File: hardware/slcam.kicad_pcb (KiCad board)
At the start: 4 copper layers, 42.2 x 25.4 mm, 33 parts, among them J1 532610671, J2 Conn_01x08, J3 Conn_01x04, J4 532610371, J5 532610371, U1 STM32F103C8Tx, U2 W25Q128JVS, U3 TCAN330G, U4 TPS2044D, Y1 Crystal_GND24

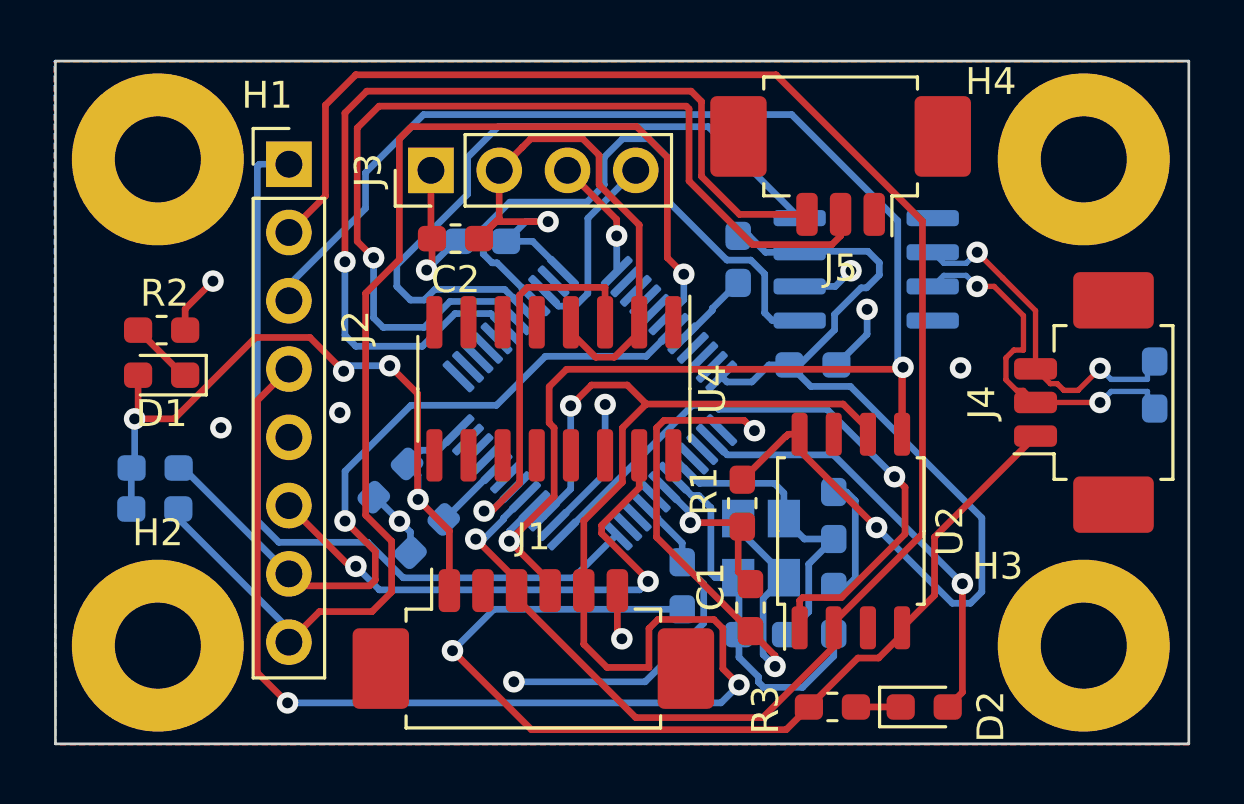
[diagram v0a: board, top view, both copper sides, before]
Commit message: hardware: Fixing DRC warnings #29
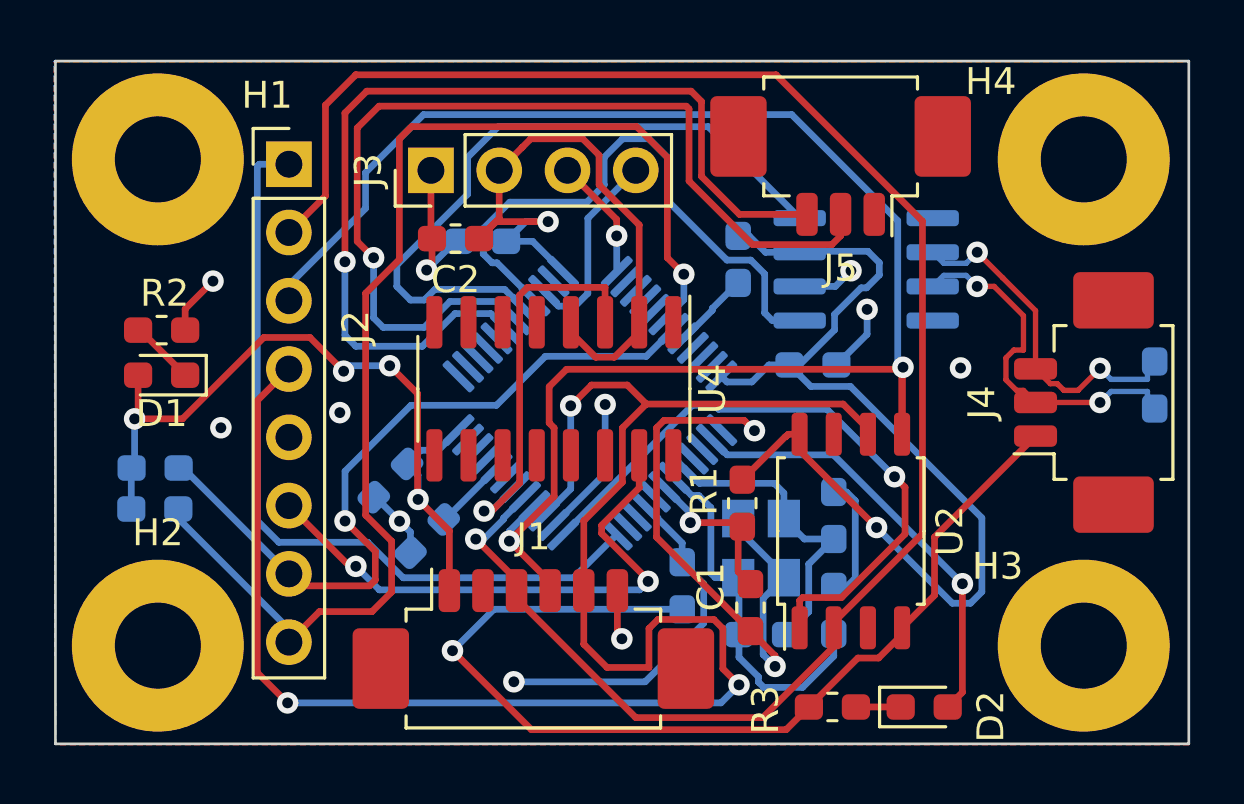
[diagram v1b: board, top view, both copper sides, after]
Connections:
- U1 pad 1: Net-(U1-Pad1) -> unconnected-(U1-Pad1)
- U1 pad 10: Net-(U1-Pad10) -> unconnected-(U1-Pad10)
- U1 pad 11: Net-(U1-Pad11) -> unconnected-(U1-Pad11)
- U1 pad 19: Net-(U1-Pad19) -> unconnected-(U1-Pad19)
- U1 pad 21: Net-(U1-Pad21) -> unconnected-(U1-Pad21)
- U1 pad 22: Net-(U1-Pad22) -> unconnected-(U1-Pad22)
- U1 pad 23: Net-(U1-Pad23) -> unconnected-(U1-Pad23)
- U1 pad 25: Net-(U1-Pad25) -> unconnected-(U1-Pad25)
- U1 pad 26: Net-(U1-Pad26) -> unconnected-(U1-Pad26)
- U1 pad 27: Net-(U1-Pad27) -> unconnected-(U1-Pad27)
- U1 pad 28: Net-(U1-Pad28) -> unconnected-(U1-Pad28)
- U1 pad 29: Net-(U1-Pad29) -> unconnected-(U1-Pad29)
- U1 pad 3: Net-(U1-Pad3) -> unconnected-(U1-Pad3)
- U1 pad 35: Net-(U1-Pad35) -> unconnected-(U1-Pad35)
- U1 pad 38: Net-(U1-Pad38) -> unconnected-(U1-Pad38)
- U1 pad 39: Net-(U1-Pad39) -> unconnected-(U1-Pad39)
- U1 pad 4: Net-(U1-Pad4) -> unconnected-(U1-Pad4)
- U1 pad 40: Net-(U1-Pad40) -> unconnected-(U1-Pad40)
- U1 pad 41: Net-(U1-Pad41) -> unconnected-(U1-Pad41)
- U1 pad 45: Net-(U1-Pad45) -> unconnected-(U1-Pad45)
- U1 pad 46: Net-(U1-Pad46) -> unconnected-(U1-Pad46)
- U1 pad 47: Net-(U1-Pad47) -> unconnected-(U1-Pad47)
- U1 pad 8: Net-(U1-Pad8) -> unconnected-(U1-Pad8)
- U2 pad 3: Net-(U2-Pad3) -> unconnected-(U2-Pad3)
- U2 pad 7: Net-(U2-Pad7) -> unconnected-(U2-Pad7)
- U3 pad 5: Net-(U3-Pad5) -> unconnected-(U3-Pad5)
- U3 pad 8: Net-(U3-Pad8) -> unconnected-(U3-Pad8)
- U4 pad 13: Net-(U4-Pad13) -> unconnected-(U4-Pad13)
- U4 pad 14: Net-(U4-Pad14) -> unconnected-(U4-Pad14)
- U4 pad 16: Net-(U4-Pad16) -> unconnected-(U4-Pad16)
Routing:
- net GND: track 145.4 -> 144.3 mm
- net VCC: track 108.4 -> 107.5 mm

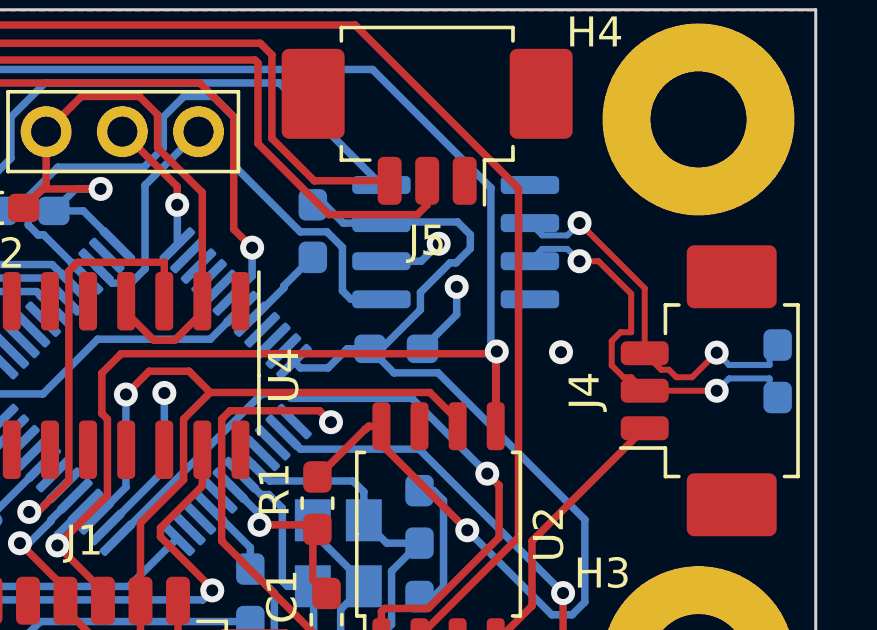
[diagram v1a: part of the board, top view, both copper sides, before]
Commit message: hardware: Adding the project name/version and the SpaceLab logo to the PCB #23 #29 closes #38 closes #42
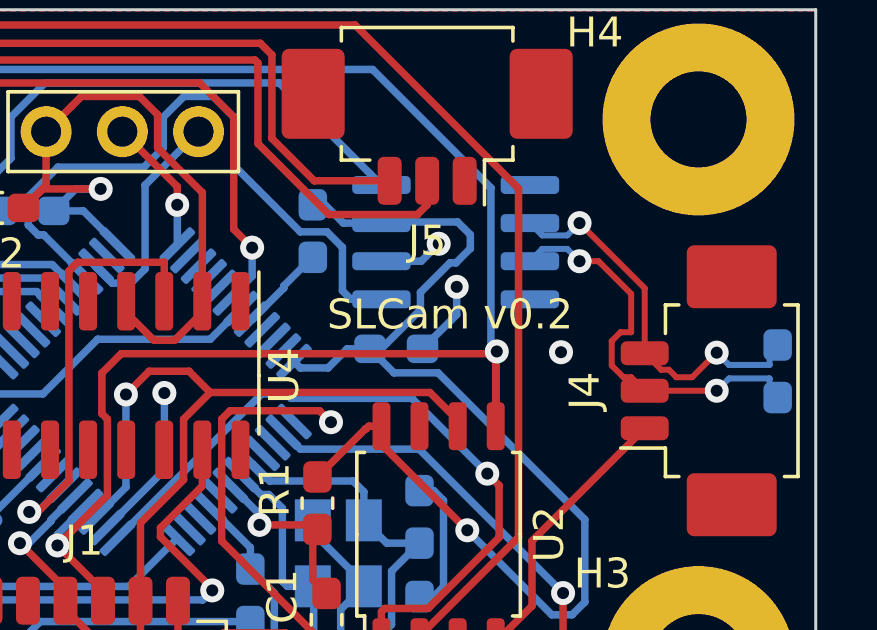
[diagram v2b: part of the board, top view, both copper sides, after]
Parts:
- added G***: LOGO, lib:spacelab-logo, B.Cu at (233.7, 62.5)
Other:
- board text added: "SLCam v0.2"

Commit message: hardware: Adding a table with info about the PCB to the layout project #29
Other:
- board text added: "0.2000 mm / 0.0000 mm"
- board text added: "0.3000 mm"
- board text added: "1.6600 mm"
- board text added: "4"
- board text added: "42.1640 mm x 25.4000 mm"
- board text added: "BOARD CHARACTERISTICS"
- board text added: "Board Thickness:"
- board text added: "Board overall dimensions:"
- board text added: "Castellated pads:"
- board text added: "Copper Finish:"
- board text added: "Copper Layer Count:"
- board text added: "Edge card connectors:"
- board text added: "Impedance Control:"
- board text added: "Min hole diameter:"
- board text added: "Min track/spacing:"
- board text added: "No"
- board text added: "None"
- board text added: "Plated Board Edge:"
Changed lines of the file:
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@@
     (effects (font (size 1 1) (thickness 0.15)))
+  )
+  (gr_text "No" (at 51.087143 37.416) (layer "Dwgs.User")
+    (effects (font (size 1.5 1.5) (thickness 0.2)) (justify left top))
+  )
+  (gr_text "42.1640 mm x 25.4000 mm" (at 51.087143 24.771) (layer "Dwgs.User")
+    (effects (font (size 1.5 1.5) (thickness 0.2)) (justify left top))
+  )
+  (gr_text "Copper Layer Count: " (at 18.53 20.556) (layer "Dwgs.User")
+    (effects (font (size 1.5 1.5) (thickness 0.2)) (justify left top))
+  )
+  (gr_text "1.6600 mm" (at 109.987143 20.556) (layer "Dwgs.User")
+    (effects (font (size 1.5 1.5) (thickness 0.2)) (justify left top))
+  )
+  (gr_text "No" (at 51.087143 41.631) (layer "Dwgs.User")
+    (effects (font (size 1.5 1.5) (thickness 0.2)) (justify left top))
+  )
+  (gr_text "Min hole diameter: " (at 85.144286 28.986) (layer "Dwgs.User")
+    (effects (font (size 1.5 1.5) (thickness 0.2)) (justify left top))
+  )
+  (gr_text "Edge card connectors: " (at 18.53 41.631) (layer "Dwgs.User")
+    (effects (font (size 1.5 1.5) (thickness 0.2)) (justify left top))
+  )
+  (gr_text "4" (at 51.087143 20.556) (layer "Dwgs.User")
+    (effects (font (size 1.5 1.5) (thickness 0.2)) (justify left top))
+  )
+  (gr_text "0.3000 mm" (at 109.987143 28.986) (layer "Dwgs.User")
+    (effects (font (size 1.5 1.5) (thickness 0.2)) (justify left top))
+  )
+  (gr_text "0.2000 mm / 0.0000 mm" (at 51.087143 28.986) (layer "Dwgs.User")
+    (effects (font (size 1.5 1.5) (thickness 0.2)) (justify left top))
+  )
+  (gr_text "No" (at 109.987143 37.416) (layer "Dwgs.User")
+    (effects (font (size 1.5 1.5) (thickness 0.2)) (justify left top))
+  )
+  (gr_text "" (at 85.144286 24.771) (layer "Dwgs.User")
+    (effects (font (size 1.5 1.5) (thickness 0.2)) (justify left top))
+  )
+  (gr_text "Plated Board Edge: " (at 85.144286 37.416) (layer "Dwgs.User")
+    (effects (font (size 1.5 1.5) (thickness 0.2)) (justify left top))
+  )
+  (gr_text "Castellated pads: " (at 18.53 37.416) (layer "Dwgs.User")
+    (effects (font (size 1.5 1.5) (thickness 0.2)) (justify left top))
+  )
+  (gr_text "No" (at 109.987143 33.201) (layer "Dwgs.User")
+    (effects (font (size 1.5 1.5) (thickness 0.2)) (justify left top))
+  )
+  (gr_text "Board overall dimensions: " (at 18.53 24.771) (layer "Dwgs.User")
+    (effects (font (size 1.5 1.5) (thickness 0.2)) (justify left top))
+  )
+  (gr_text "" (at 109.987143 24.771) (layer "Dwgs.User")
+    (effects (font (size 1.5 1.5) (thickness 0.2)) (justify left top))
+  )
+  (gr_text "BOARD CHARACTERISTICS" (at 17.78 14.986) (layer "Dwgs.User")
+    (effects (font (size 2 2) (thickness 0.4)) (justify left top))
+  )
+  (gr_text "Min track/spacing: " (at 18.53 28.986) (layer "Dwgs.User")
+    (effects (font (size 1.5 1.5) (thickness 0.2)) (justify left top))
+  )
+  (gr_text "Impedance Control: " (at 85.144286 33.201) (layer "Dwgs.User")
+    (effects (font (size 1.5 1.5) (thickness 0.2)) (justify left top))
+  )
+  (gr_text "None" (at 51.087143 33.201) (layer "Dwgs.User")
+    (effects (font (size 1.5 1.5) (thickness 0.2)) (justify left top))
+  )
+  (gr_text "Board Thickness: " (at 85.144286 20.556) (layer "Dwgs.User")
+    (effects (font (size 1.5 1.5) (thickness 0.2)) (justify left top))
+  )
+  (gr_text "Copper Finish: " (at 18.53 33.201) (layer "Dwgs.User")
+    (effects (font (size 1.5 1.5) (thickness 0.2)) (justify left top))
   )
   (dimension (type aligned) (layer "Dwgs.User")
@@
     )
   )
+  (group "group-boardCharacteristics" (id 049aa7e6-b220-43d7-bba0-bdc17c67ffca)
+    (members
+      0423cd57-9fdd-41b7-88d0-eff59a4796ae
+      09736371-8c49-4408-be6b-c6217fe9588f
+      2f660782-9c07-4859-a507-79267764da2e
+      3b806a2a-4c44-40fa-8d4a-b45d74612247
+      504059e5-24d8-4cde-aa50-b4f6f2668e30
+      6fe74c89-3b2e-4c5e-9d37-58837c106d12
+      8f3ae896-f9e1-4488-96b4-a0e2e031a533
+      939005bf-1497-4782-b6a7-5841c7bee1c7
+      96dd2630-2dd7-4a49-a035-95ab511dddde
+      984227ab-5b44-45fc-8356-319beba366c4
+      9896f9af-9a15-4800-8ef8-7983e6617c77
+      ab3b54eb-9236-44c1-b05c-9191b8f09a87
+      ac40669b-43b3-46c4-a1d6-d67504f652b3
+      afea4d71-11ad-4c21-b793-d26fbfef74f8
+      b3f2b68d-26ce-4f0c-9596-4a19558e3f30
+      b4f40a7b-b48f-4590-bfd9-29912e1b92db
+      b51a09a8-40c2-4ff1-99a3-d41a462b81b9
+      c0d1a491-5f04-49f5-a484-fcb9958ae31c
+      cfef0d70-c128-43bc-971d-1f13e4e52832
+      dd09d0da-55e3-45ea-afed-6746aeeb9bb2
+      eb3e51a2-dd97-4c08-8f7b-249bbd43a78a
+      f5f04ec6-d2c1-48b8-9f77-a02d7375a629
+      fbc4a301-0019-42a2-bd27-a34e1e73f4d0
+    )
+  )

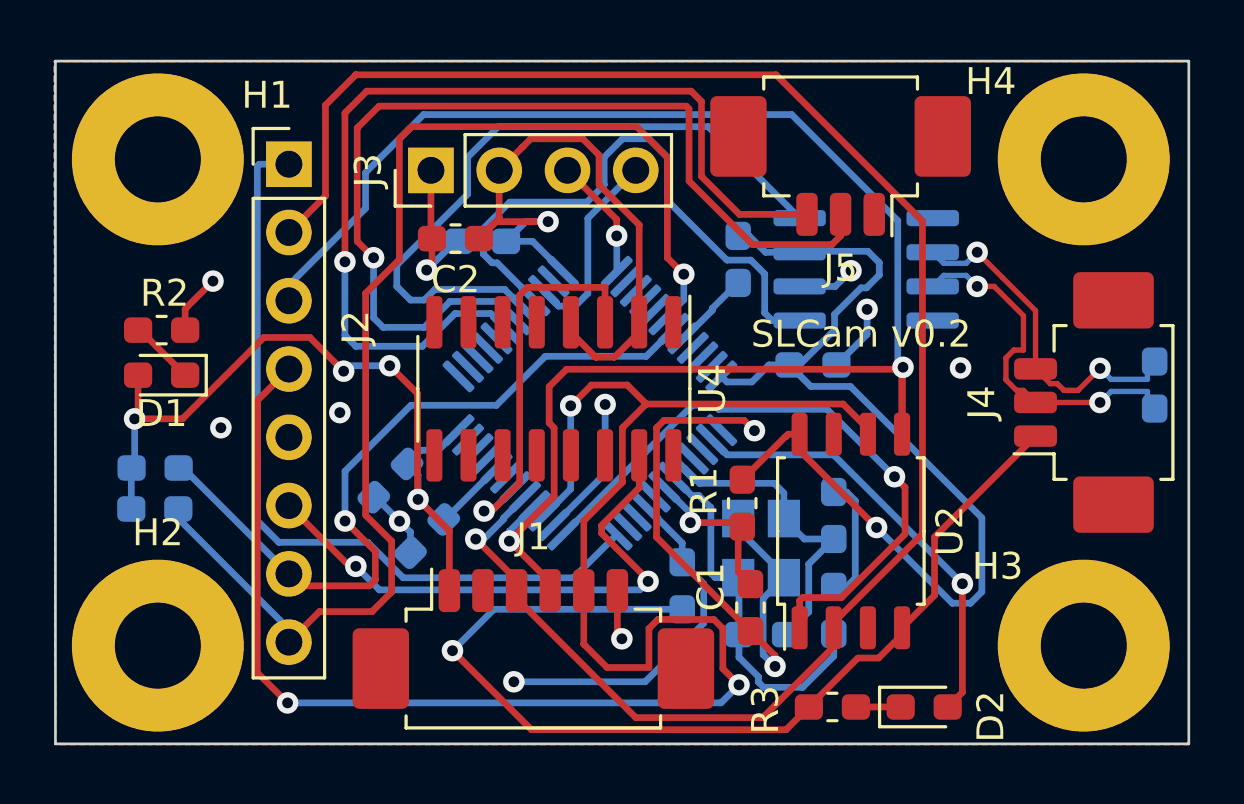
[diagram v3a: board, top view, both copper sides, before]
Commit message: hardware: Updating the layout with the connections of the second part of the TPS2044D IC #28
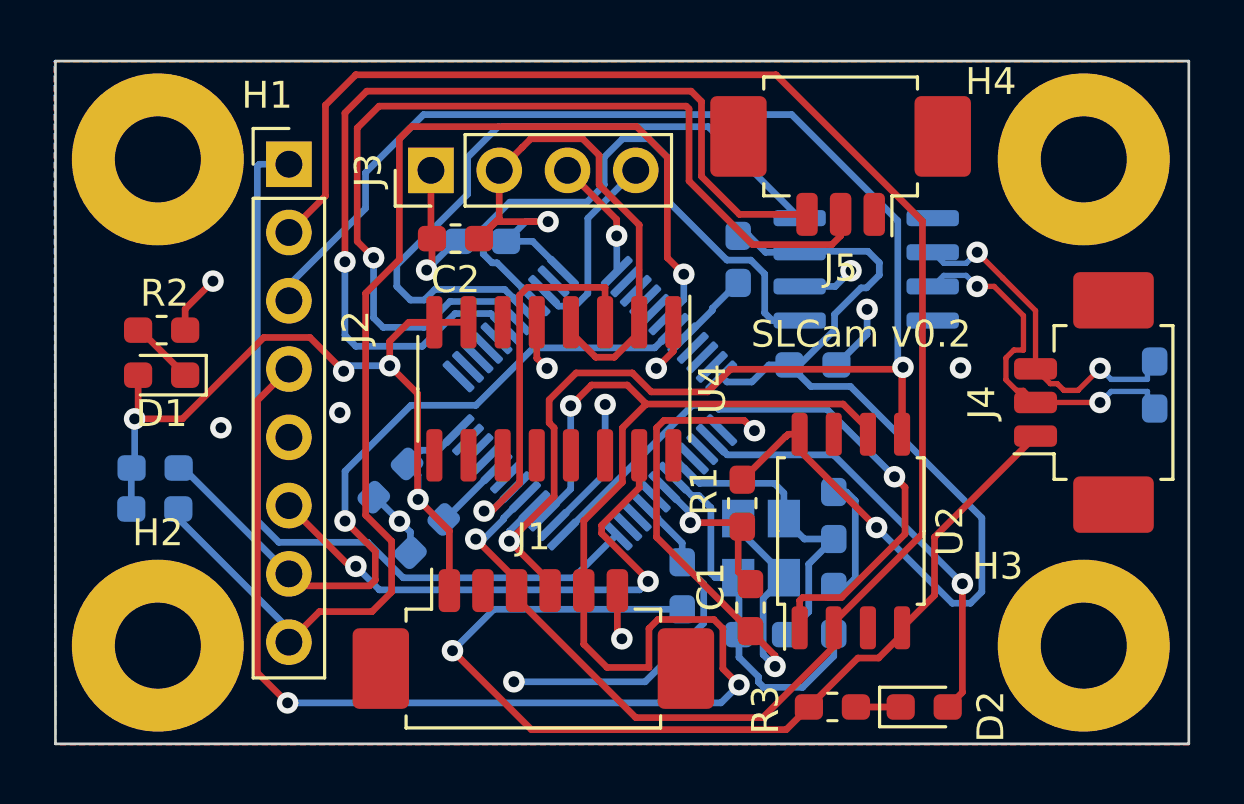
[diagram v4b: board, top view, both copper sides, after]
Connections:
- U4 pad 10: (no net) -> unconnected-(U4-Pad10)
- U4 pad 11: (no net) -> unconnected-(U4-Pad11)
- U4 pad 12: (no net) -> unconnected-(U4-Pad12)
- U4 pad 5: (no net) -> GND
- U4 pad 6: (no net) -> unconnected-(U4-Pad6)
- U4 pad 7: (no net) -> VCC
- U4 pad 8: (no net) -> VCC
- U4 pad 9: (no net) -> unconnected-(U4-Pad9)
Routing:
- net VCC: track 107.5 -> 111.6 mm
- net GND: track 144.3 -> 148.2 mm, vias 11 -> 13
